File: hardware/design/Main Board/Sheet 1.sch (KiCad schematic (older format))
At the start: 1 part

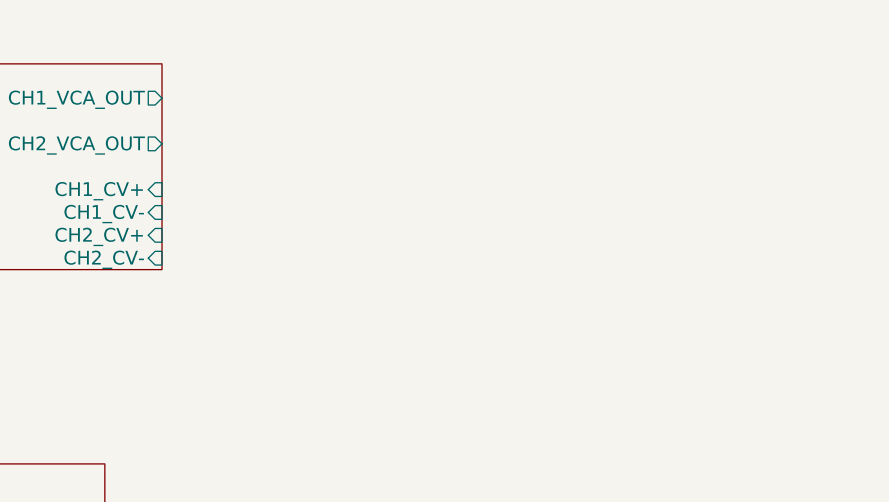
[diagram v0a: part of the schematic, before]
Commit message: Main PCB Design
Added Output Stage
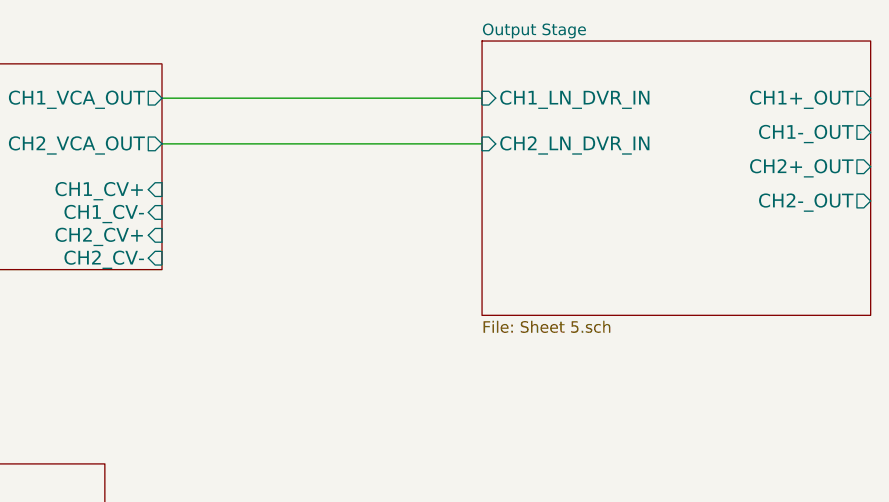
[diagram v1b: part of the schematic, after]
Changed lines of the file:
@@
 $Descr A4 11693 8268
 encoding utf-8
-Sheet 1 4
+Sheet 1 5
 Title ""
-Date "16 apr 2014"
+Date "17 apr 2014"
 Rev ""
 Comp ""
@@
 Wire Wire Line
 	2600 4550 2900 4550
+$Sheet
+S 6200 2250 1700 1200
+U 534F2525
+F0 "Output Stage" 50
+F1 "Sheet 5.sch" 50
+F2 "CH1_LN_DVR_IN" I L 6200 2500 60
+F3 "CH1+_OUT" O R 7900 2500 60
+F4 "CH1-_OUT" O R 7900 2650 60
+F5 "CH2_LN_DVR_IN" I L 6200 2700 60
+F6 "CH2+_OUT" O R 7900 2800 60
+F7 "CH2-_OUT" O R 7900 2950 60
+$EndSheet
+Wire Wire Line
+	4800 2500 6200 2500
+Wire Wire Line
+	4800 2700 6200 2700
 $EndSCHEMATC

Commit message: Op Amp Changes
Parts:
- added P?: CONN_4, symbol CONN_4
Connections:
- net Output Stage/CH1+_OUT: now also P?.1 (P1)
- net Output Stage/CH1-_OUT: now also P?.2 (P2)
- net Output Stage/CH2+_OUT: now also P?.3 (P3)
- net Output Stage/CH2-_OUT: now also P?.4 (P4)
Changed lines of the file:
@@
 $Descr A4 11693 8268
 encoding utf-8
-Sheet 1 5
+Sheet 1 6
 Title ""
-Date "29 apr 2014"
+Date "2 may 2014"
 Rev ""
 Comp ""
@@
 	1500 2750 1700 2750
 $Sheet
-S 2900 4100 1650 700
+S 4450 4150 1650 700
 U 534DCE54
 F0 "Precision Rectifier" 50
 F1 "Sheet 3.sch" 50
-F2 "CH1_RECT_IN" I L 2900 4300 60
-F3 "CH2_RECT_IN" I L 2900 4550 60
-F4 "CH1_RECT_OUT" O R 4550 4300 60
-F5 "CH2_RECT_OUT" O R 4550 4550 60
+F2 "CH1_RECT_IN" I L 4450 4350 60
+F3 "CH2_RECT_IN" I L 4450 4600 60
+F4 "CH1_RECT_OUT" O R 6100 4350 60
+F5 "CH2_RECT_OUT" O R 6100 4600 60
 $EndSheet
 Wire Wire Line
 	2550 2700 3350 2700
 Wire Wire Line
-	2600 2700 2600 4550
-Wire Wire Line
 	2550 2500 3350 2500
-Wire Wire Line
-	2700 2500 2700 4300
 $Sheet
 S 3350 2350 1450 900
@@
 F9 "CH2_CV+" I R 4800 3100 60
 $EndSheet
-Connection ~ 2700 2500
-Connection ~ 2600 2700
-Wire Wire Line
-	2700 4300 2900 4300
-Wire Wire Line
-	2600 4550 2900 4550
 $Sheet
 S 6200 2250 1700 1200
@@
 F2 "CH1_LN_DVR_IN" I L 6200 2500 60
 F3 "CH1+_OUT" O R 7900 2500 60
-F4 "CH1-_OUT" O R 7900 2650 60
+F4 "CH1-_OUT" O R 7900 2600 60
 F5 "CH2_LN_DVR_IN" I L 6200 2700 60
-F6 "CH2+_OUT" O R 7900 2800 60
-F7 "CH2-_OUT" O R 7900 2950 60
+F6 "CH2+_OUT" O R 7900 2700 60
+F7 "CH2-_OUT" O R 7900 2800 60
 $EndSheet
 Wire Wire Line
@@
 Wire Wire Line
 	4800 2700 6200 2700
+$Comp
+L CONN_4 P?
+U 1 1 5362E417
+P 8950 2650
+F 0 "P?" V 8900 2650 50  0000 C CNN
+F 1 "CONN_4" V 9000 2650 50  0000 C CNN
+F 2 "" H 8950 2650 60  0000 C CNN
+F 3 "" H 8950 2650 60  0000 C CNN
+	1    8950 2650
+	1    0    0    -1
+$EndComp
+$Sheet
+S 3050 4150 1150 700
+U 5362F285
+F0 "LPF" 50
+F1 "Sheet 6.sch" 50
+F2 "LPF_IN_1" I L 3050 4350 60
+F3 "LPF_IN_2" I L 3050 4600 60
+F4 "LPF_OUT_1" O R 4200 4350 60
+F5 "LPF_OUT_2" O R 4200 4600 60
+$EndSheet
+Wire Wire Line
+	3050 4350 2750 4350
+Wire Wire Line
+	2750 4350 2750 2500
+Connection ~ 2750 2500
+Wire Wire Line
+	2650 2700 2650 4600
+Wire Wire Line
+	2650 4600 3050 4600
+Connection ~ 2650 2700
+Wire Wire Line
+	4200 4350 4450 4350
+Wire Wire Line
+	4200 4600 4450 4600
+Wire Wire Line
+	8600 2500 7900 2500
+Wire Wire Line
+	8600 2600 7900 2600
+Wire Wire Line
+	8600 2700 7900 2700
+Wire Wire Line
+	8600 2800 7900 2800
 $EndSCHEMATC
